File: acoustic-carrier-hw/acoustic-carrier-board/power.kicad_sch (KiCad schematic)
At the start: 79 parts, among them IC1 ECP5-BGA256, J3 Conn_02x08_Odd_Even, U10 TLV62569DBV, U11 TLV62569DBV, U14 TLV62569DBV, U5 OPA376xxDBV, U8 TLV62569DBV

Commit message: [carrier] Finished switch and reverse voltage circuit
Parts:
- removed D1, D6: SS54, Diode_SMD:D_SMA, symbol Device:D_Schottky
- removed L6: 100@100MHz, Inductor_SMD:L_0805_2012Metric, symbol Device:L_Small
- removed R46: 0, Resistor_SMD:R_0805_2012Metric_Pad1.20x1.40mm_HandSolder, symbol Device:R_Small
- added C16: 0.1uF, Capacitor_SMD:C_0402_1005Metric, symbol Device:C_Small
- added C17: 150uF, Capacitor_SMD:CP_Elec_8x6.2, symbol Device:C_Polarized_Small
- added Q1: AO3401A, Package_TO_SOT_SMD:SOT-23, symbol Transistor_FET:AO3401A
- added R11: 100k, Resistor_SMD:R_0603_1608Metric_Pad0.98x0.95mm_HandSolder, symbol Device:R_Small
- added R12: 27k, Resistor_SMD:R_0603_1608Metric, symbol Device:R_Small
- added R13, R16: 5.1k, Resistor_SMD:R_0603_1608Metric, symbol Device:R_Small
- added R14, R15: 24k, Resistor_SMD:R_0603_1608Metric, symbol Device:R_Small
- added R17: 22k, Resistor_SMD:R_0603_1608Metric, symbol Device:R_Small
- added TP9: TestPoint, symbol Connector:TestPoint
- added U16: TPS2121RUX, iw-power:TPS2121, symbol iw-power:TPS2121RUXR
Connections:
- net +5V: now also C17.1, U16.1 (OUT), U16.8 (OUT)
- net BP_5V: now also Q1.2 (S)
- net GND: now also C16.2, C17.2, R11.2, R12.1, R13.2, R16.2, R17.2, U16.12 (GND), U16.3 (CP2), U16.6 (PR1)
- net USB_VBUS: now also R14.1, U16.7 (IN1)
- new net: R15.2, R16.1, U16.4 (OV2)
- new net: Q1.1 (G), R17.1
- new net: Q1.3 (D), R15.1, U16.2 (IN2)
- new net: R13.1, R14.2, U16.5 (OV1)
- new net: R12.2, U16.10 (ILM)
- new net: C16.1, U16.11 (SS)
- new net: R11.1, TP9.1, U16.9 (ST)
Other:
- note added: "REVERSE VOLTAGE PROTECTION MOSFET - Imax: 5.7 A - Vgs_max 12 V - Rdson: 85m-50m ANODE / CATHODE source drain connection - Switched around, becuase normally input: voltage regulator - Main thing: Vgs high enough -> pushed high anyways"
- note added: "R_ILM: - 27 kOhm, current limiting [4 amps] SS: - Settling time, time to wait for the switch to open once input voltage is valid - 0.1 uF: 780 V / s -> 6.4 ms OP1/2: - Voltage reference (1.01 .. 1.1) - When OP1/2 input > reference => turned off / channel switch - Choose 5.1, 22 kOhm VDIV -> 1.05 / [5.1 / (24+5.1)] = 6 V PR: - Connect to GND (not req) CP2: - Enables comparator operation (external 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"
- note removed: "Add resistance in case of high inrush current"
- moved on the sheet: C10, C11, C12, C13, C14, C15, C18, C19, C20, C21, C26, C27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

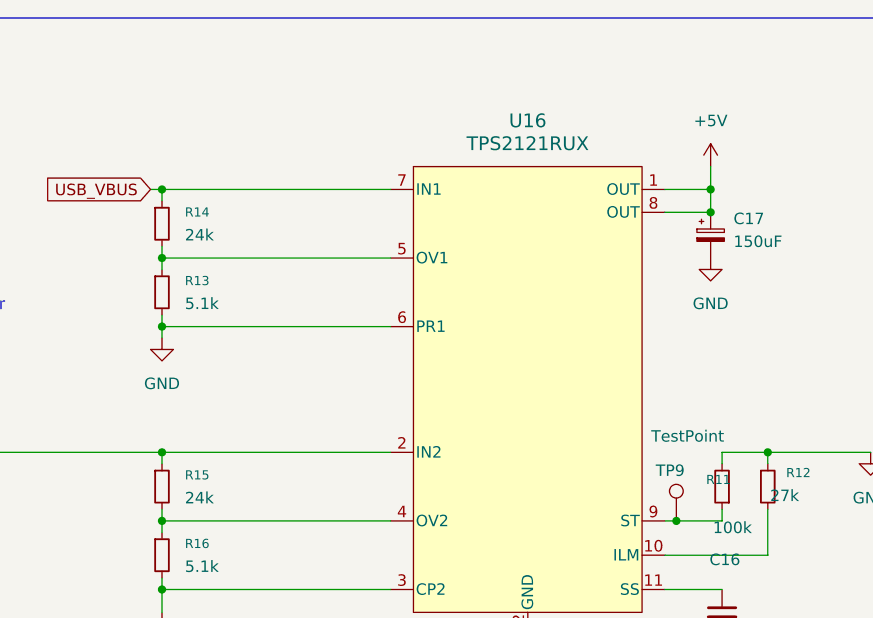
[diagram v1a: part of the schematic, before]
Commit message: [carrier] Signal switch-around in ddr3
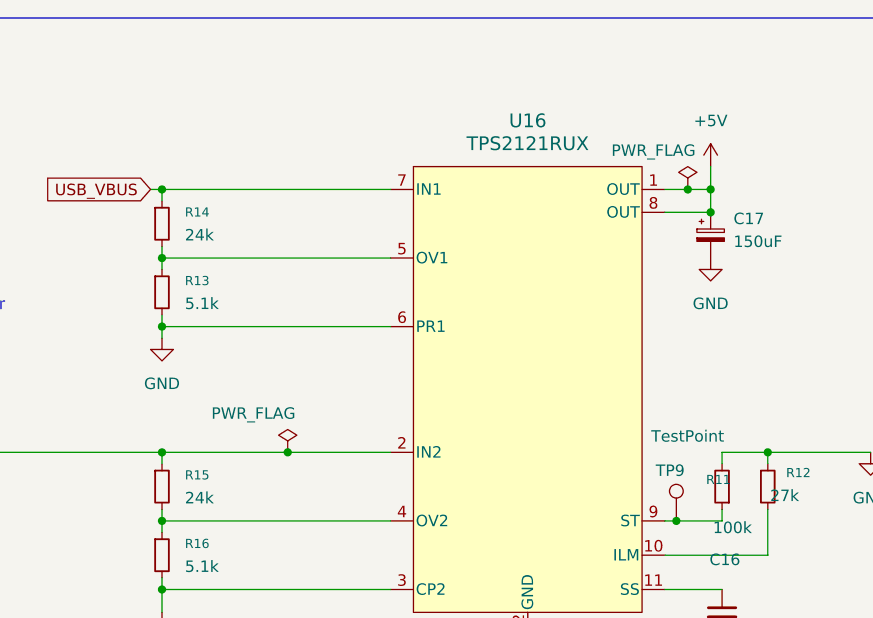
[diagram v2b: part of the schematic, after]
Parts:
- TP9: footprint (none) -> TestPoint:TestPoint_Pad_1.0x1.0mm
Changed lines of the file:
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@@
 	)
 	(junction
+		(at 198.12 43.18)
+		(diameter 0)
+		(color 0 0 0 0)
+	)
+	(junction
 		(at 148.59 142.24)
 		(diameter 0)
@@
 	)
 	(junction
+		(at 153.67 72.39)
+		(diameter 0)
+		(color 0 0 0 0)
+	)
+	(junction
 		(at 273.05 220.98)
 		(diameter 0)
@@
 	(wire
 		(pts
+			(xy 153.67 72.39) (xy 165.1 72.39)
+		)
+		(stroke
+			(width 0)
+			(type default)
+		)
+	)
+	(wire
+		(pts
 			(xy 128.27 212.09) (xy 128.27 214.63)
 		)
@@
 	(wire
 		(pts
-			(xy 195.58 43.18) (xy 200.66 43.18)
+			(xy 195.58 43.18) (xy 198.12 43.18)
 		)
 		(stroke
@@
 	(wire
 		(pts
+			(xy 198.12 43.18) (xy 200.66 43.18)
+		)
+		(stroke
+			(width 0)
+			(type default)
+		)
+	)
+	(wire
+		(pts
 			(xy 68.58 198.12) (xy 68.58 201.93)
 		)
@@
 	(wire
 		(pts
-			(xy 139.7 72.39) (xy 165.1 72.39)
+			(xy 139.7 72.39) (xy 153.67 72.39)
 		)
 		(stroke
@@
 	(symbol
 		(lib_id "power:PWR_FLAG")
+		(at 153.67 72.39 0)
+		(unit 1)
+		(exclude_from_sim no)
+		(in_bom yes)
+		(on_board yes)
+		(dnp no)
+		(property "Reference" "#FLG021"
+			(at 153.67 70.485 0)
+			(effects
+				(font
+					(size 1.27 1.27)
+				)
+				(hide yes)
+			)
+		)
+		(property "Value" "PWR_FLAG"
+			(at 149.86 68.072 0)
+			(effects
+				(font
+					(size 1.27 1.27)
+				)
+			)
+		)
+		(property "Footprint" ""
+			(at 153.67 72.39 0)
+			(effects
+				(font
+					(size 1.27 1.27)
+				)
+				(hide yes)
+			)
+		)
+		(property "Datasheet" "~"
+			(at 153.67 72.39 0)
+			(effects
+				(font
+					(size 1.27 1.27)
+				)
+				(hide yes)
+			)
+		)
+		(property "Description" "Special symbol for telling ERC where power comes from"
+			(at 153.67 72.39 0)
+			(effects
+				(font
+					(size 1.27 1.27)
+				)
+				(hide yes)
+			)
+		)
+		(pin "1"
+		)
+		(instances
+			(project "acoustic-carrier-board"
+				(path "/25b015c9-ab13-4427-b72c-b6f348597100/aad6bec2-3cac-4ef0-abf0-8e1f80301155"
+					(reference "#FLG021")
+					(unit 1)
+				)
+			)
+		)
+	)
+	(symbol
+		(lib_id "power:PWR_FLAG")
 		(at 102.87 247.65 0)
 		(unit 1)
@@
 	)
 	(symbol
+		(lib_id "power:PWR_FLAG")
+		(at 198.12 43.18 0)
+		(unit 1)
+		(exclude_from_sim no)
+		(in_bom yes)
+		(on_board yes)
+		(dnp no)
+		(property "Reference" "#FLG014"
+			(at 198.12 41.275 0)
+			(effects
+				(font
+					(size 1.27 1.27)
+				)
+				(hide yes)
+			)
+		)
+		(property "Value" "PWR_FLAG"
+			(at 194.31 38.862 0)
+			(effects
+				(font
+					(size 1.27 1.27)
+				)
+			)
+		)
+		(property "Footprint" ""
+			(at 198.12 43.18 0)
+			(effects
+				(font
+					(size 1.27 1.27)
+				)
+				(hide yes)
+			)
+		)
+		(property "Datasheet" "~"
+			(at 198.12 43.18 0)
+			(effects
+				(font
+					(size 1.27 1.27)
+				)
+				(hide yes)
+			)
+		)
+		(property "Description" "Special symbol for telling ERC where power comes from"
+			(at 198.12 43.18 0)
+			(effects
+				(font
+					(size 1.27 1.27)
+				)
+				(hide yes)
+			)
+		)
+		(pin "1"
+		)
+		(instances
+			(project "acoustic-carrier-board"
+				(path "/25b015c9-ab13-4427-b72c-b6f348597100/aad6bec2-3cac-4ef0-abf0-8e1f80301155"
+					(reference "#FLG014")
+					(unit 1)
+				)
+			)
+		)
+	)
+	(symbol
 		(lib_id "Device:C_Small")
 		(at 129.54 198.12 0)
@@
 			)
 		)
-		(property "Footprint" ""
+		(property "Footprint" "TestPoint:TestPoint_Pad_1.0x1.0mm"
 			(at 201.93 80.01 0)
 			(effects

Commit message: [carrier] Added hierarchical labels
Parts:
- removed C10, C11, C12, C13, C14, C26, C31, C41, C7, C74, C75, C8, C9: 10uF, Capacitor_SMD:C_0603_1608Metric, symbol Device:C_Small
- removed C15: 47uF, Capacitor_SMD:C_0805_2012Metric, symbol Device:C_Small
- removed C16, C33, C36, C45, C48, C50, C51, C52, C61, C62, C63, C64, C65, C66: 0.1uF, Capacitor_SMD:C_0402_1005Metric, symbol Device:C_Small
- removed C17: 150uF, Capacitor_SMD:CP_Elec_8x6.2, symbol Device:C_Polarized_Small
- removed C18, C19, C20, C21: 10pF, Capacitor_SMD:C_0402_1005Metric, symbol Device:C_Small
- removed C27, C28, C29, C69, C76: 4.7uF, Capacitor_SMD:C_0402_1005Metric, symbol Device:C_Small
- removed C53, C60: 470nF, Capacitor_SMD:C_0603_1608Metric, symbol Device:C_Small
- removed C54, C55, C56, C68: 1uF, Capacitor_SMD:C_0805_2012Metric, symbol Device:C_Small
- removed IC1: ECP5-BGA256, iw-fpga_mcu:BGA256C80P16X16_1400X1400X170, symbol iw-fpga_mcu:ECP5-BGA256
- removed J3: Conn_02x08_Odd_Even, Connector_PinSocket_2.54mm:PinSocket_2x08_P2.54mm_Horizontal, symbol Connector_Generic:Conn_02x08_Odd_Even
- removed L1, L2, L3, L7: 2.2uH, iw-inductor:L_Changjiang_FNR4018S, symbol Device:L_Small
- removed Q1: AO3401A, Package_TO_SOT_SMD:SOT-23, symbol Transistor_FET:AO3401A
- removed R100: 220, Resistor_SMD:R_0603_1608Metric, symbol Device:R_Small
- removed R11: 100k, Resistor_SMD:R_0603_1608Metric_Pad0.98x0.95mm_HandSolder, symbol Device:R_Small
- removed R12: 27k, Resistor_SMD:R_0603_1608Metric, symbol Device:R_Small
- removed R13, R16: 5.1k, Resistor_SMD:R_0603_1608Metric, symbol Device:R_Small
- removed R14, R15: 24k, Resistor_SMD:R_0603_1608Metric, symbol Device:R_Small
- removed R17: 22k, Resistor_SMD:R_0603_1608Metric, symbol Device:R_Small
- removed R3, R6, R7, R8: 0, Resistor_SMD:R_0805_2012Metric_Pad1.20x1.40mm_HandSolder, symbol Device:R_Small
- removed R4, R5, R56: 1k, Resistor_SMD:R_0603_1608Metric, symbol Device:R_Small
- removed R59, R63: 24k, Resistor_SMD:R_0603_1608Metric, symbol Device:R
- removed R60, R99: 0, Resistor_SMD:R_0603_1608Metric, symbol Device:R_Small
- removed R61, R64, R65: 100k, Resistor_SMD:R_0402_1005Metric, symbol Device:R
- removed R62: 22k, Resistor_SMD:R_0603_1608Metric, symbol Device:R
- removed R97: 75k, Resistor_SMD:R_0603_1608Metric, symbol Device:R
- removed R98: 30k, Resistor_SMD:R_0603_1608Metric, symbol Device:R
- removed TP4, TP5, TP6, TP7: TestPoint_Small, TestPoint:TestPoint_Pad_D1.5mm, symbol Connector:TestPoint_Small
- removed TP9: TestPoint, TestPoint:TestPoint_Pad_1.0x1.0mm, symbol Connector:TestPoint
- removed U10, U11, U14, U8: TLV62569DBV, Package_TO_SOT_SMD:SOT-23-5, symbol Regulator_Switching:TLV62569DBV
- removed U16: TPS2121RUX, iw-power:TPS2121, symbol iw-power:TPS2121RUXR
- removed U5: OPA376xxDBV, Package_TO_SOT_SMD:SOT-23-5, symbol Amplifier_Operational:OPA376xxDBV
- added C143, C157, C169, C179: 1uF, Capacitor_SMD:C_0805_2012Metric, symbol Device:C_Small
- added C144, C158, C171, C180, C79: 4.7uF, Capacitor_SMD:C_0402_1005Metric, symbol Device:C_Small
- added C154, C170, C175, C81: 10pF, Capacitor_SMD:C_0402_1005Metric, symbol Device:C_Small
- added C155, C156, C166, C167, C168, C176, C177, C178, C44, C78, C85: 10uF, Capacitor_SMD:C_0603_1608Metric, symbol Device:C_Small
- added C22: 150uF, Capacitor_SMD:CP_Elec_8x6.2, symbol Device:C_Polarized_Small
- added C25: 0.1uF, Capacitor_SMD:C_0402_1005Metric, symbol Device:C_Small
- added L13, L14, L15, L6: 2.2uH, iw-inductor:L_Changjiang_FNR4018S, symbol Device:L_Small
- added Q2: AO3401A, Package_TO_SOT_SMD:SOT-23, symbol Transistor_FET:AO3401A
- added R18, R26: 5.1k, Resistor_SMD:R_0603_1608Metric, symbol Device:R_Small
- added R19, R9: 24k, Resistor_SMD:R_0603_1608Metric, symbol Device:R_Small
- added R21: 100k, Resistor_SMD:R_0603_1608Metric_Pad0.98x0.95mm_HandSolder, symbol Device:R_Small
- added R24: 27k, Resistor_SMD:R_0603_1608Metric, symbol Device:R_Small
- added R25: 22k, Resistor_SMD:R_0603_1608Metric, symbol Device:R_Small
- added R27, R28, R33, R50: 0, Resistor_SMD:R_0805_2012Metric_Pad1.20x1.40mm_HandSolder, symbol Device:R_Small
- added R29, R30, R32: 100k, Resistor_SMD:R_0402_1005Metric, symbol Device:R
- added R31: 22k, Resistor_SMD:R_0603_1608Metric, symbol Device:R
- added R34: 75k, Resistor_SMD:R_0603_1608Metric, symbol Device:R
- added R46, R71: 24k, Resistor_SMD:R_0603_1608Metric, symbol Device:R
- added R55: 30k, Resistor_SMD:R_0603_1608Metric, symbol Device:R
- added R66, R76, R77: 1k, Resistor_SMD:R_0603_1608Metric, symbol Device:R_Small
- added R68, R70: 0, Resistor_SMD:R_0603_1608Metric, symbol Device:R_Small
- added R72: 220, Resistor_SMD:R_0603_1608Metric, symbol Device:R_Small
- added TP1: TestPoint, TestPoint:TestPoint_Pad_1.0x1.0mm, symbol Connector:TestPoint
- added TP2: TestPoint_Small, TestPoint:TestPoint_Pad_D1.5mm, symbol Connector:TestPoint_Small
- added U17: TPS2121RUX, iw-power:TPS2121, symbol iw-power:TPS2121RUXR
- added U19, U21, U24, U25: TLV62569DBV, Package_TO_SOT_SMD:SOT-23-5, symbol Regulator_Switching:TLV62569DBV
- added U26: OPA376xxDBV, Package_TO_SOT_SMD:SOT-23-5, symbol Amplifier_Operational:OPA376xxDBV
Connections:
- net +1V2: now also C154.1, C155.1, C156.1, C157.1, L13.2, R28.1, R30.2
- net +1V35: now also C175.1, C176.1, C177.1, C178.1, C179.1, L15.2, R50.1, R55.2
- net +2V5: now also C166.1, C167.1, C168.1, C169.1, C170.1, L14.2, R33.1, R34.2
- net +3V3: now also C143.1, C44.1, C78.1, C79.1, C81.1, C85.1, L6.2, R27.1, R29.2, TP2.1
- net +5V: now also C144.1, C158.1, C171.1, C180.1, C22.1, U17.1 (OUT), U17.8 (OUT), U19.1 (EN), U19.4 (VIN), U21.1 (EN), U21.4 (VIN), U24.1 (EN), U24.4 (VIN), U25.1 (EN), U25.4 (VIN), U26.5 (V+)
- net BP_5V: now also Q2.2 (S)
- net GND: now also C143.2, C144.2, C155.2, C156.2, C157.2, C158.2, C166.2, C167.2, C168.2, C169.2, C171.2, C176.2, C177.2, C178.2, C179.2, C180.2, C22.2, C25.2, C44.2, C78.2, C79.2, C85.2, R18.2, R21.2, R24.1, R25.2, R26.2, R31.1, R32.1, R46.1, R71.1, R76.2, R77.1, U17.12 (GND), U17.3 (CP2), U17.6 (PR1), U19.2 (GND), U21.2 (GND), U24.2 (GND), U25.2 (GND), U26.2 (V-)
- net USB_VBUS: now also R9.1, U17.7 (IN1)
- net VAUX_2V5: now also R33.2
- net VCORE_3V3: now also R27.2
- net VDDR3L_0.675: now also R68.2, R72.1
- net VDDR3L_1.35: now also R50.2, R66.1
- net VETH_1V2: now also R28.2
- new net: C81.2, R29.1, R31.2, U19.5 (FB)
- new net: R18.1, R9.2, U17.5 (OV1)
- new net: C154.2, R30.1, R32.2, U21.5 (FB)
- new net: Q2.3 (D), R19.1, U17.2 (IN2)
- new net: R19.2, R26.1, U17.4 (OV2)
- new net: C175.2, R55.1, R71.2, U25.5 (FB)
- new net: C25.1, U17.11 (SS)
- new net: C170.2, R34.1, R46.2, U24.5 (FB)
- new net: L6.1, U19.3 (SW)
- new net: R24.2, U17.10 (ILM)
- new net: R21.1, TP1.1, U17.9 (ST)
- new net: Q2.1 (G), R25.1
- new net: L15.1, U25.3 (SW)
- new net: L14.1, U24.3 (SW)
- new net: R72.2, R77.2, U26.1, U26.4 (-)
- new net: R70.1, U26.3 (+)
- new net: L13.1, U21.3 (SW)
- new net: R66.2, R68.1, R70.2, R76.1
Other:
- note added: "DDR3L / BANK SUPPLY VOLTAGE AND REFERENCE"
- note added: "ETHERNET POWER SUPPLY"
- note removed: "Bank 2, 6 PIO supply voltage (DDR3L)"
- note removed: "Ethernet Supply Voltage"
- note removed: "FPGA POWER"
- note removed: "PIO DECOUPLING"
- note removed: "Power Board (power connector)"
- note removed: "R2 value: - Make sure the R2's are all < 200 kOhm (datasheet recommendations) Capacitor - f_zero = 1/(2*pi*R2*10e-12) = 159 kHz for 100 kOhm, 10 pF - Response time for fb loop decreases by 50 % compared to 6.8 pF case R2/R1 ratio: - 0.6 * (1+R1/R2) = Vout"

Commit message: [carrier] Added decoupling caps to flash and comparators
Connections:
- net VDDR3L_0.675 renamed VLPDDR3_0.675
- net VDDR3L_1.35 renamed VLPDDR3_1.35
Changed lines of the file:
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@@
+	(wire
+		(pts
+			(xy 158.75 245.11) (xy 162.56 245.11)
+		)
+		(stroke
+			(width 0)
+			(type default)
+		)
+	)
 	(wire
 		(pts
@@
 	(wire
 		(pts
+			(xy 217.17 245.11) (xy 223.52 245.11)
+		)
+		(stroke
+			(width 0)
+			(type default)
+		)
+	)
+	(wire
+		(pts
 			(xy 82.55 134.62) (xy 82.55 138.43)
 		)
@@
 		)
 	)
-	(global_label "VDDR3L_1.35"
+	(global_label "VLPDDR3_0.675"
 		(shape passive)
-		(at 110.49 246.38 0)
+		(at 162.56 245.11 0)
 		(fields_autoplaced yes)
 		(effects
@@
 		)
 		(property "Intersheetrefs" "${INTERSHEET_REFS}"
-			(at 124.701 246.38 0)
-			(effects
-				(font
-					(size 1.27 1.27)
-				)
-				(justify left)
-				(hide yes)
-			)
-		)
-	)
-	(global_label "VDDR3L_0.675"
-		(shape passive)
-		(at 158.75 245.11 0)
-		(fields_autoplaced yes)
-		(effects
-			(font
-				(size 1.27 1.27)
-			)
-			(justify left)
-		)
-		(property "Intersheetrefs" "${INTERSHEET_REFS}"
-			(at 174.1705 245.11 0)
+			(at 179.2505 245.11 0)
 			(effects
 				(font
@@
 		)
 	)
-	(global_label "VDDR3L_0.675"
+	(global_label "VLPDDR3_1.35"
 		(shape passive)
-		(at 223.52 245.11 180)
+		(at 110.49 246.38 0)
 		(fields_autoplaced yes)
 		(effects
@@
 				(size 1.27 1.27)
 			)
-			(justify right)
+			(justify left)
 		)
 		(property "Intersheetrefs" "${INTERSHEET_REFS}"
-			(at 208.0995 245.11 0)
+			(at 125.971 246.38 0)
 			(effects
 				(font
 					(size 1.27 1.27)
 				)
-				(justify right)
+				(justify left)
 				(hide yes)
 			)
@@
 		)
 	)
-	(global_label "VDDR3L_1.35"
+	(global_label "VLPDDR3_0.675"
 		(shape passive)
-		(at 179.07 251.46 0)
+		(at 217.17 245.11 180)
 		(fields_autoplaced yes)
 		(effects
@@
 				(size 1.27 1.27)
 			)
-			(justify left)
+			(justify right)
 		)
 		(property "Intersheetrefs" "${INTERSHEET_REFS}"
-			(at 193.281 251.46 0)
+			(at 200.4795 245.11 0)
 			(effects
 				(font
 					(size 1.27 1.27)
 				)
-				(justify left)
+				(justify right)
 				(hide yes)
 			)
@@
 			(effects
 				(font
+					(size 1.27 1.27)
+				)
+				(justify left)
+				(hide yes)
+			)
+		)
+	)
+	(global_label "VLPDDR3_1.35"
+		(shape passive)
+		(at 179.07 251.46 0)
+		(fields_autoplaced yes)
+		(effects
+			(font
+				(size 1.27 1.27)
+			)
+			(justify left)
+		)
+		(property "Intersheetrefs" "${INTERSHEET_REFS}"
+			(at 194.551 251.46 0)
+			(effects
+				(font

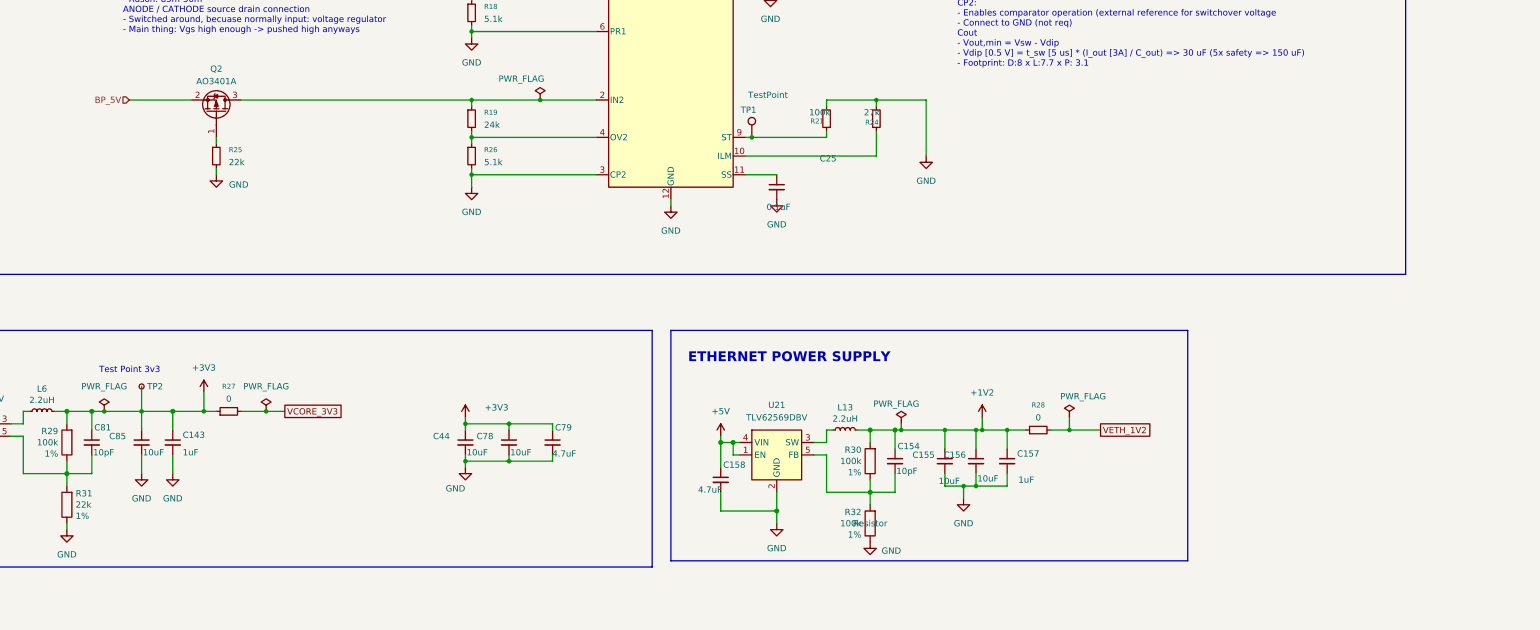
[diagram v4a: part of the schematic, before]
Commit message: [carrier] Added extra decoupling to ECP5U according to datasheet (next) perform page-wise checks, add testpoints
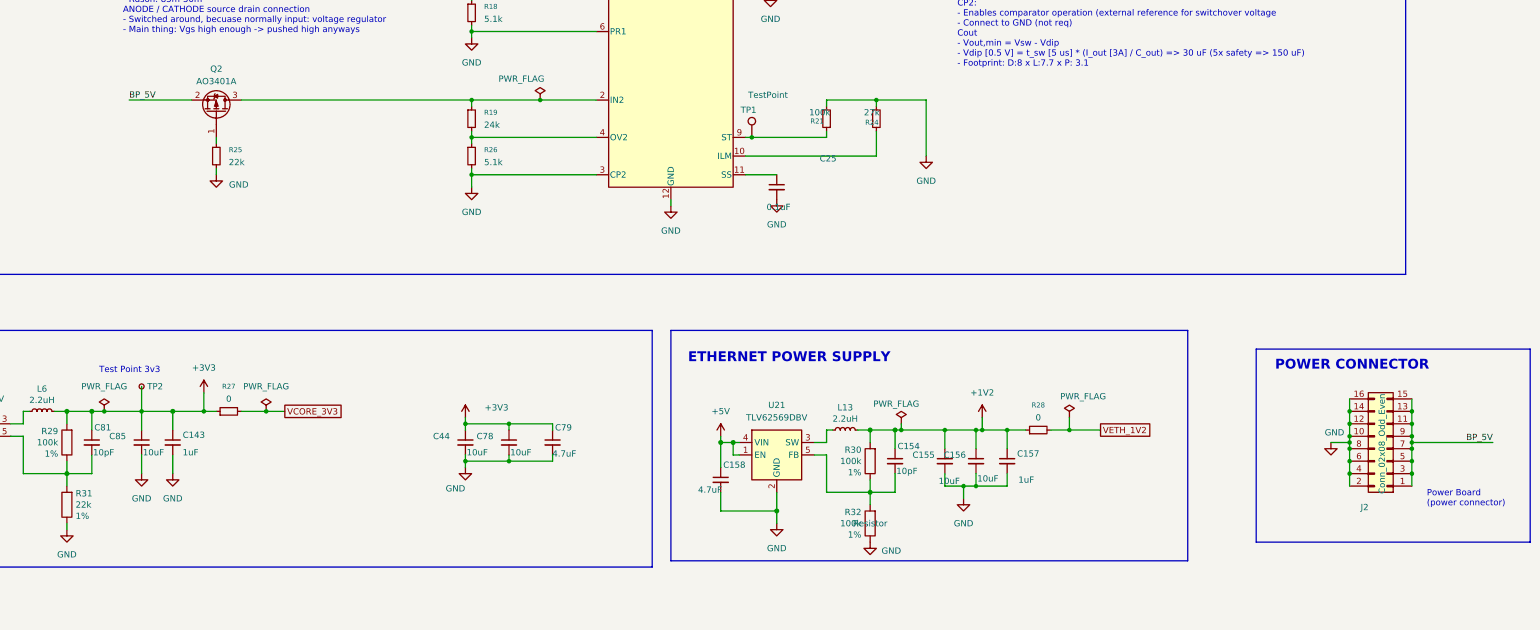
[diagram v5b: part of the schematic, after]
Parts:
- added J2: Conn_02x08_Odd_Even, Connector_PinSocket_2.54mm:PinSocket_2x08_P2.54mm_Horizontal, symbol Connector_Generic:Conn_02x08_Odd_Even
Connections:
- net BP_5V: now also J2.1 (Pin_1), J2.11 (Pin_11), J2.13 (Pin_13), J2.15 (Pin_15), J2.3 (Pin_3), J2.5 (Pin_5), J2.7 (Pin_7), J2.9 (Pin_9)
- net GND: now also J2.10 (Pin_10), J2.12 (Pin_12), J2.14 (Pin_14), J2.16 (Pin_16), J2.2 (Pin_2), J2.4 (Pin_4), J2.6 (Pin_6), J2.8 (Pin_8)
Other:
- note added: "POWER CONNECTOR"
- note added: "Power Board (power connector)"
